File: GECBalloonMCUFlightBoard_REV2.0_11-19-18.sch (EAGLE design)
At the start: 52 parts, among them IC1 PIC32MX360F512L, U1 ADS1118, U2 ADS1118, X2 MALE_VGA, Y1 SG-636PCW_50.0000MC3__ROHS

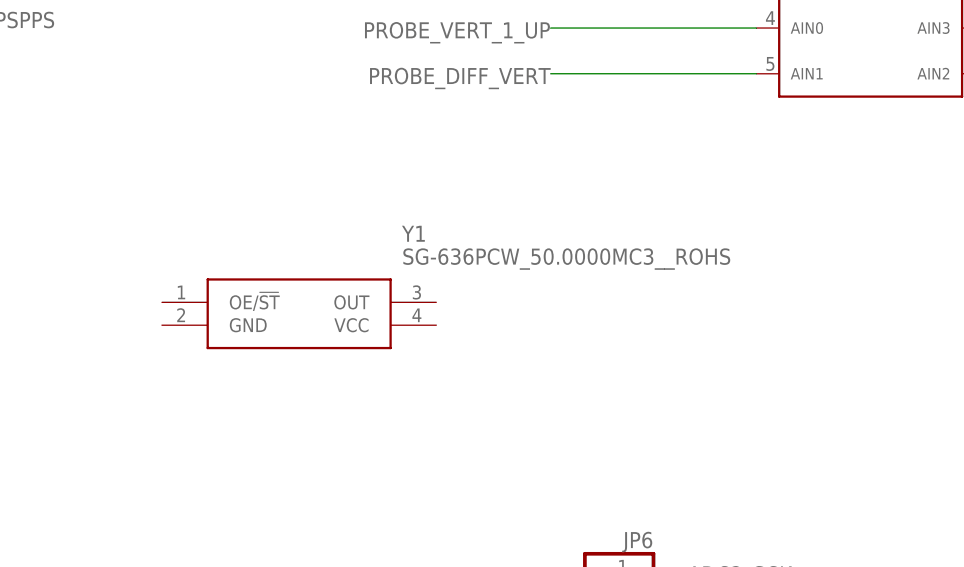
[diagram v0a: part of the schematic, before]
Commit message: COnnected GPSPPS pin and Incremented revision number
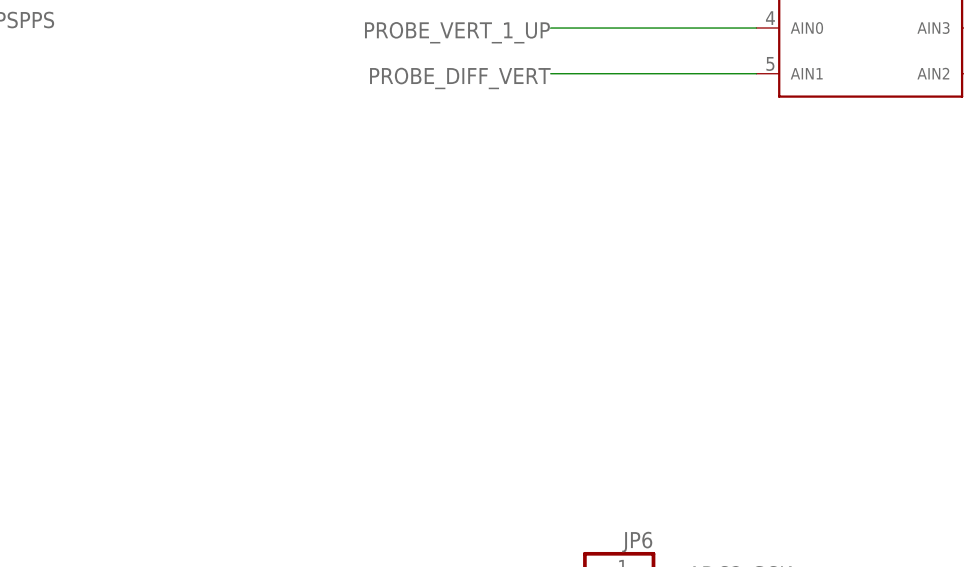
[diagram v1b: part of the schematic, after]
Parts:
- removed Y1: SG-636PCW_50.0000MC3__ROHS, SG-636PCW_50.0000MC3__ROHS:SG-636PCW_50.0000MC3__ROHS
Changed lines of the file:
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@@
 <part name="R4" library="resistor" deviceset="R-US_" device="0414/15" value="1k"/>
 <part name="R8" library="resistor" deviceset="R-US_" device="0414/15" value="1k"/>
-<part name="Y1" library="SG-636PCW_50.0000MC3__ROHS" deviceset="SG-636PCW_50.0000MC3__ROHS" device=""/>
 </parts>
 <sheets>
@@
 <instance part="R4" gate="G$1" x="139.7" y="12.7" rot="R180"/>
 <instance part="R8" gate="G$1" x="144.78" y="5.08" rot="R180"/>
-<instance part="Y1" gate="G$1" x="177.8" y="132.08"/>
 </instances>
 <busses>
